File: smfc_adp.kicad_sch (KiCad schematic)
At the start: 22 parts, among them U1 ADP5091

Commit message: WIP
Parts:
- added J1, J2, J3: Conn_01x04_Socket, Connector_PinHeader_2.54mm:PinHeader_1x04_P2.54mm_Vertical, symbol Connector:Conn_01x04_Socket
- added JP1, JP2: SolderJumper_3_Bridged12, Jumper:SolderJumper-3_P1.3mm_Bridged12_Pad1.0x1.5mm, symbol Jumper:SolderJumper_3_Bridged12
- added R1: 55.6k, Resistor_SMD:R_0603_1608Metric_Pad0.98x0.95mm_HandSolder, symbol Device:R_US
- C1, C2, C3, C4, C5, C6, C?: footprint (none) -> Capacitor_SMD:C_0603_1608Metric_Pad1.08x0.95mm_HandSolder
- R10: renamed from R9; footprint (none) -> Resistor_SMD:R_0603_1608Metric_Pad0.98x0.95mm_HandSolder
- R11: renamed from R10; footprint (none) -> Resistor_SMD:R_0603_1608Metric_Pad0.98x0.95mm_HandSolder
- R12: renamed from R11; footprint (none) -> Resistor_SMD:R_0603_1608Metric_Pad0.98x0.95mm_HandSolder
- R13: renamed from R12; footprint (none) -> Resistor_SMD:R_0603_1608Metric_Pad0.98x0.95mm_HandSolder
- R14: renamed from R13; footprint (none) -> Resistor_SMD:R_0603_1608Metric_Pad0.98x0.95mm_HandSolder
- R2: renamed from R1; footprint (none) -> Resistor_SMD:R_0603_1608Metric_Pad0.98x0.95mm_HandSolder
- R3: renamed from R2; footprint (none) -> Resistor_SMD:R_0603_1608Metric_Pad0.98x0.95mm_HandSolder
- R4: renamed from R3; footprint (none) -> Resistor_SMD:R_0603_1608Metric_Pad0.98x0.95mm_HandSolder
- R5: renamed from R4; footprint (none) -> Resistor_SMD:R_0603_1608Metric_Pad0.98x0.95mm_HandSolder
- R6: renamed from R5; footprint (none) -> Resistor_SMD:R_0603_1608Metric_Pad0.98x0.95mm_HandSolder
- R7: renamed from R6; footprint (none) -> Resistor_SMD:R_0603_1608Metric_Pad0.98x0.95mm_HandSolder
- R8: renamed from R7; footprint (none) -> Resistor_SMD:R_0603_1608Metric_Pad0.98x0.95mm_HandSolder
- R9: renamed from R8; footprint (none) -> Resistor_SMD:R_0603_1608Metric_Pad0.98x0.95mm_HandSolder
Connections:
- net +BATT: now also J1.1 (Pin_1), J1.2 (Pin_2)
- net GND: now also J1.3 (Pin_3), J1.4 (Pin_4), J3.1 (Pin_1), J3.2 (Pin_2), J3.3 (Pin_3), J3.4 (Pin_4), JP1.3 (B), JP2.2 (C), R1.1; no longer U1.24 (REG_D0)
- net SYS: now also JP1.2 (C), JP2.3 (B); no longer U1.23 (REG_D1)
- net V_{ADP}: now also J2.1 (Pin_1), J2.2 (Pin_2), J2.3 (Pin_3), J2.4 (Pin_4)
- net at U1.20 (VID): now also R1.2
- new net: JP1.1 (A), U1.23 (REG_D1)
- new net: JP2.1 (A), U1.24 (REG_D0)
- no-connect marks 4 -> 3
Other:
- note added: "18/(18+4.7) = 0.793 MPPT set-point configured to around 80% of open circuit voltage"
- note added: "I need to confirm, but I think we can disable the regulated output by setting REG_D1 and D2 to GND"
- note added: "REG_FB is unused, effectively, as we're using VID to set the voltage for REG_OUT (that said, do we just want to disable REG_OUT?)."
- note added: "Settings for all of the control pins: SETSD - Sets shutdown discharge voltage on BAT pin - ~1.011 * (5.9 / 4.12 + 1) = between 2.32, 2.59 V due to V_{INT_REF} tolerance While BAT voltage < SETSD setpoint, converter is in async mode SETBK - Sets backup voltage enable threshold - ~ 1.011 * (6.04/4.02 + 1) = between 2.39 and 2.67 V due to V_{INT_REF} While BAT voltage < SETBK setpoint, backup batter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"
- note added: "Should we experiment and try powering our system from SYS instead of BAT? SYS is what charges up BAT."
- note added: "VID: floating, it sets reg output to 2.5V. Use a 55.6k resistor to set it to 3.3V."

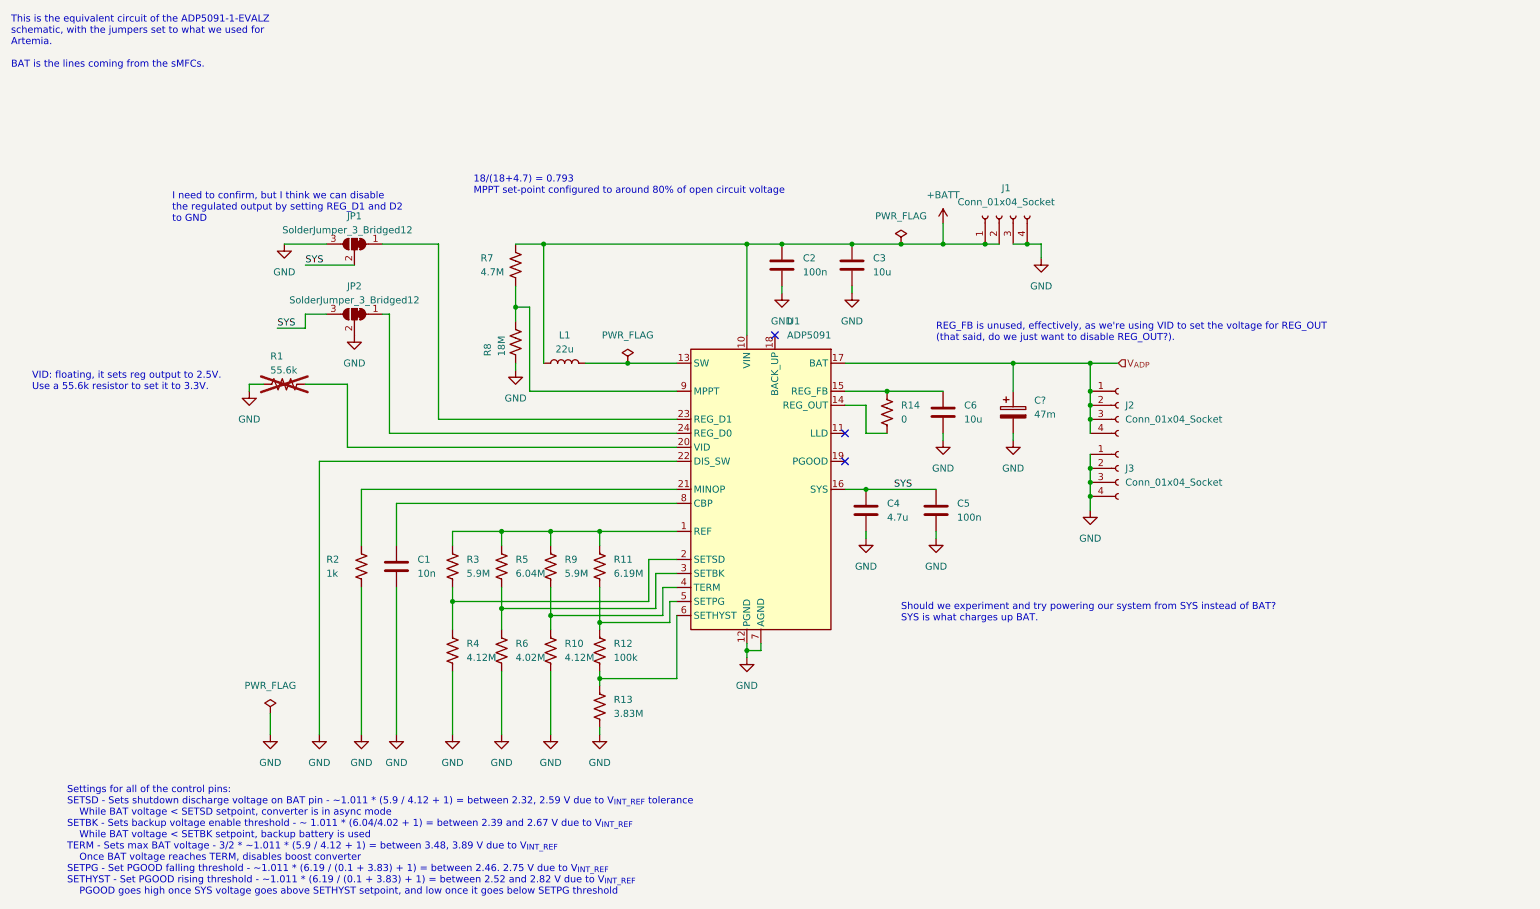
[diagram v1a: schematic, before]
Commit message: Layout cleanups, add more component data
 - Selected part for USB C socket
 - Tried to make more of the schematics compact and modular
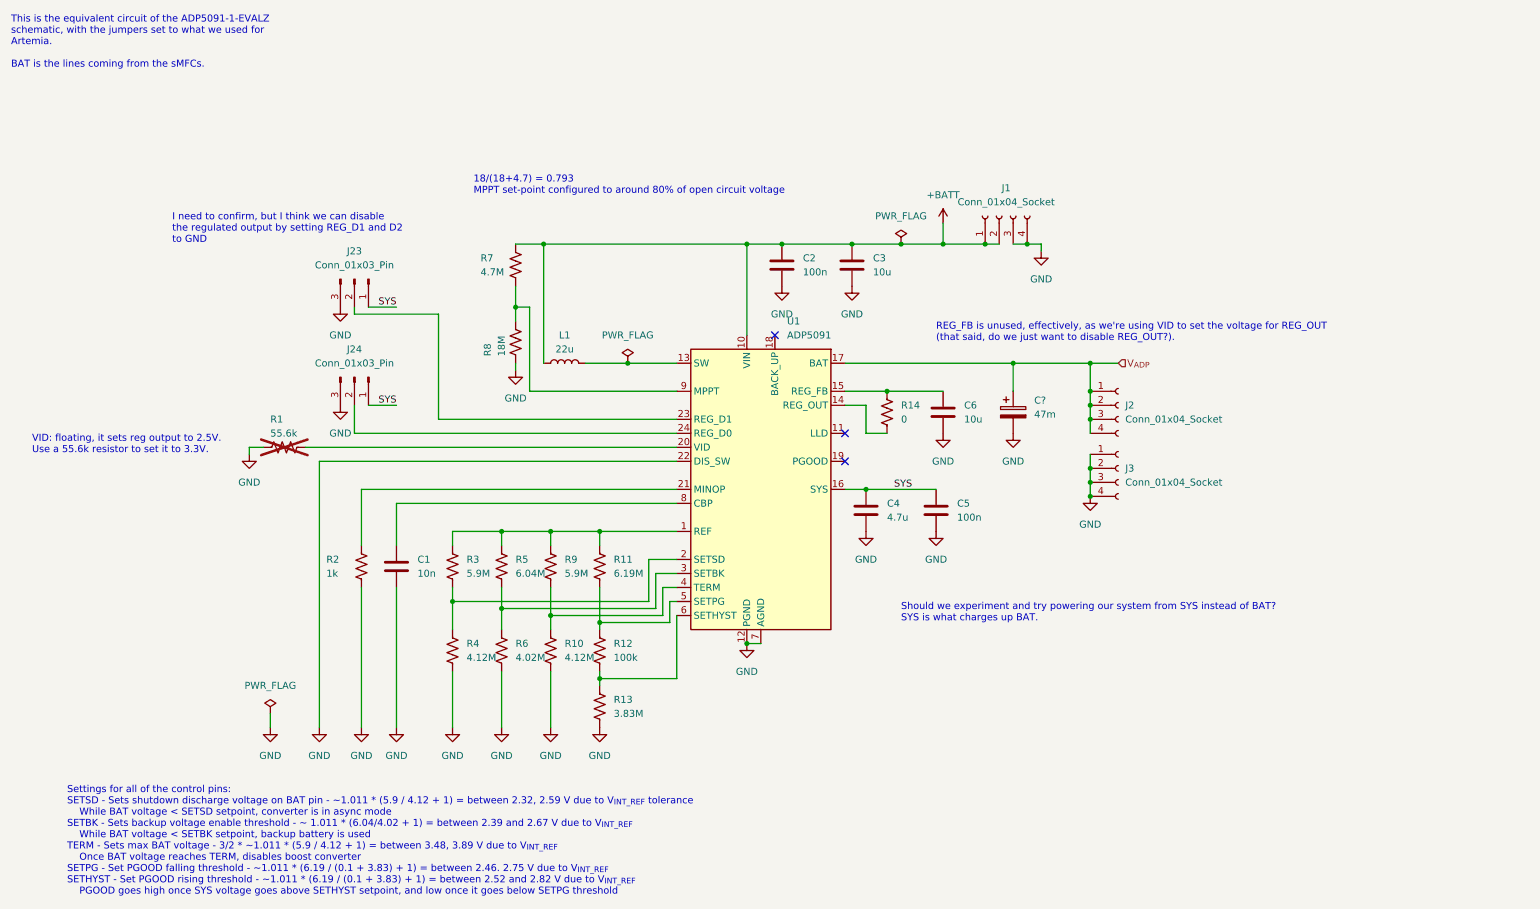
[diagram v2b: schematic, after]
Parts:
- removed JP1, JP2: SolderJumper_3_Bridged12, Jumper:SolderJumper-3_P1.3mm_Bridged12_Pad1.0x1.5mm, symbol Jumper:SolderJumper_3_Bridged12
- added J23, J24: Conn_01x03_Pin, Connector_PinHeader_2.54mm:PinHeader_1x03_P2.54mm_Vertical, symbol Connector:Conn_01x03_Pin
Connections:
- net GND: now also J23.3 (Pin_3), J24.3 (Pin_3)
- net SYS: now also J23.1 (Pin_1), J24.1 (Pin_1)
- net at U1.23 (REG_D1): now also J23.2 (Pin_2)
- net at U1.24 (REG_D0): now also J24.2 (Pin_2)
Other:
- moved on the sheet: R1

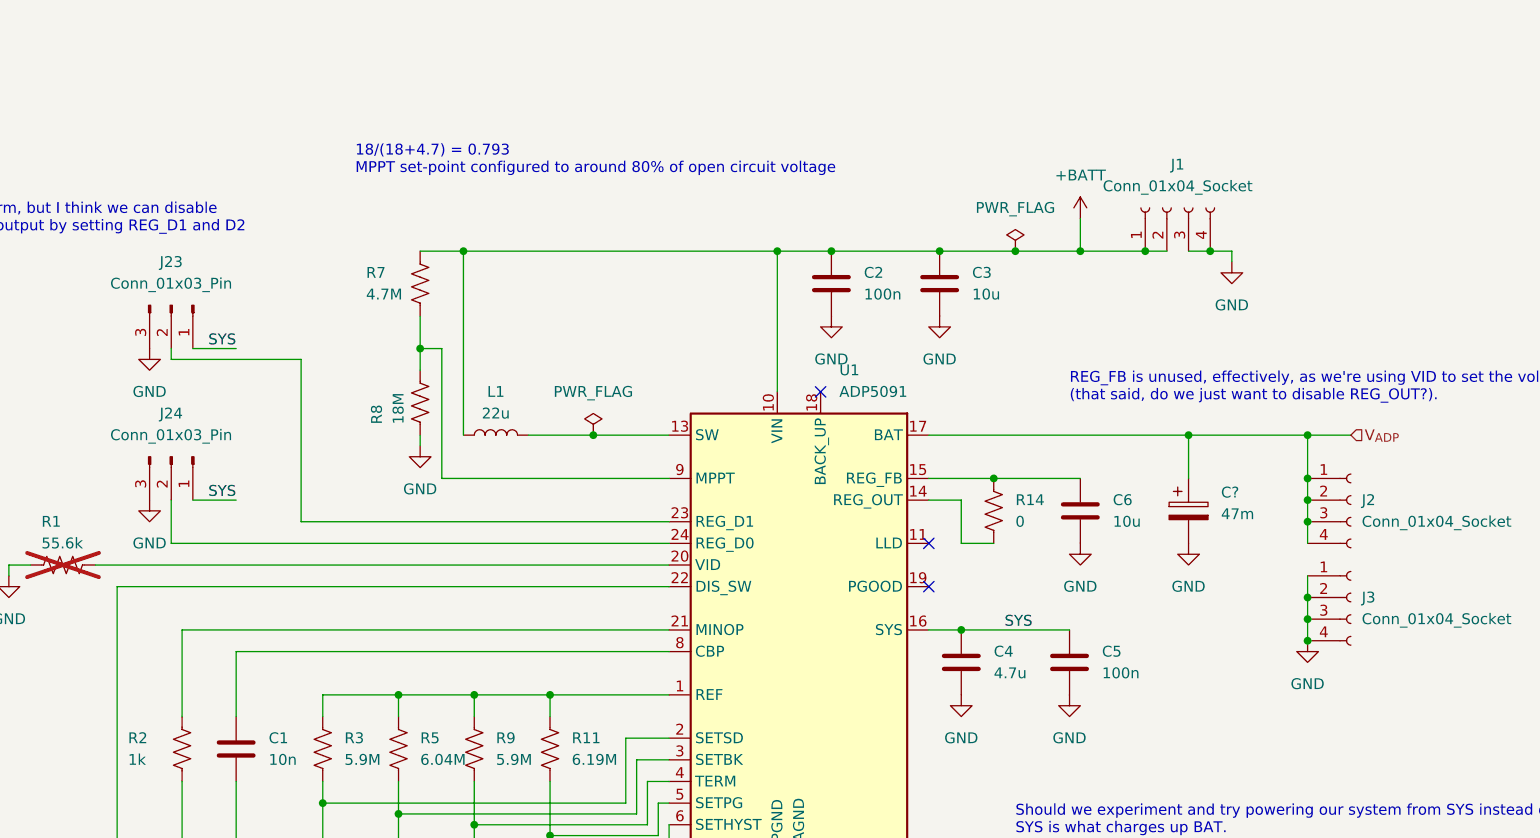
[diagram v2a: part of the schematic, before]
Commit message: First routing attempt
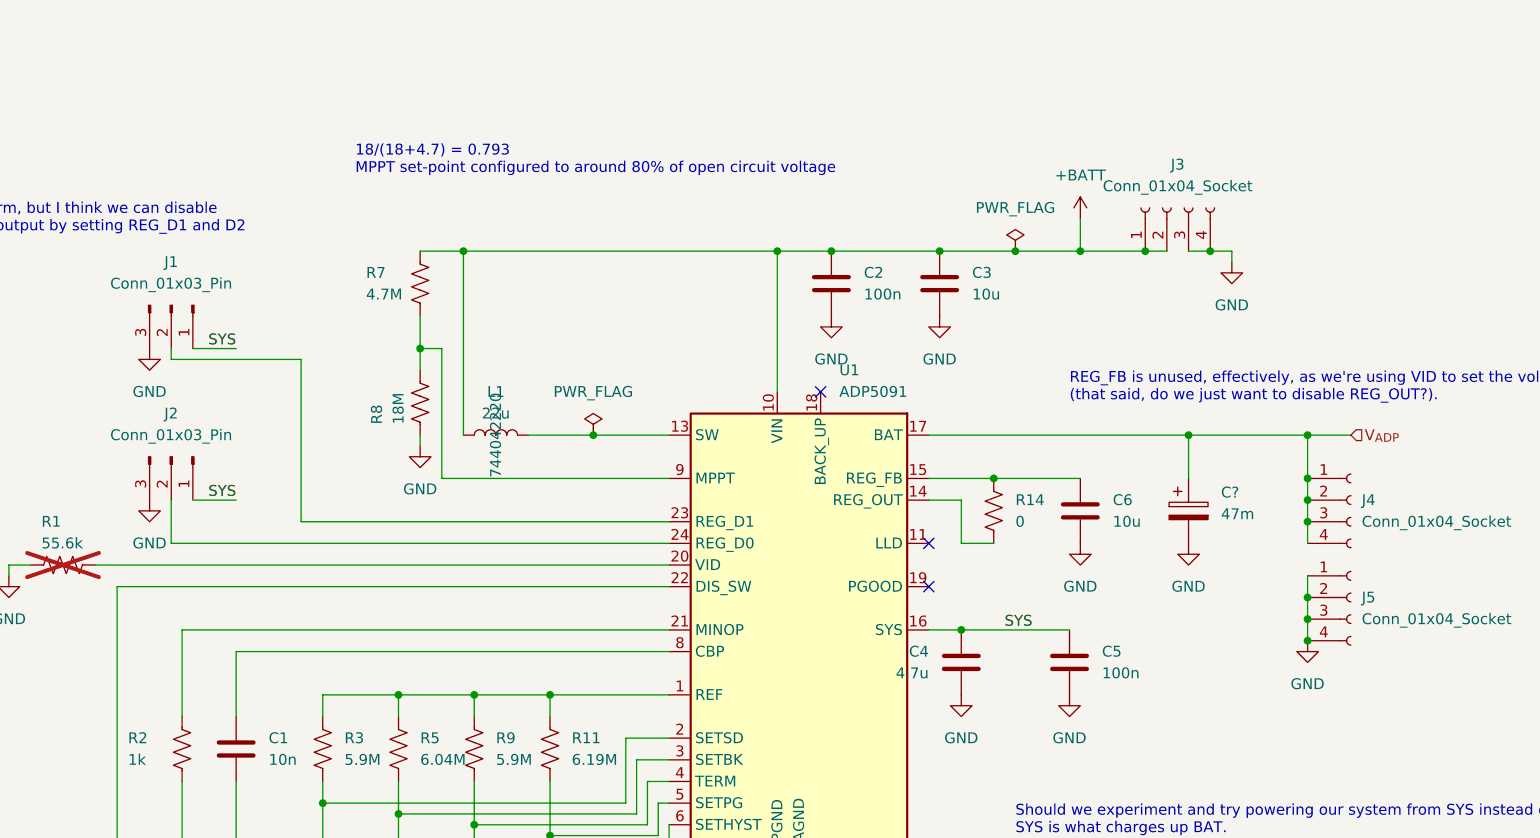
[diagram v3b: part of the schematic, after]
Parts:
- C?: footprint Capacitor_SMD:C_0603_1608Metric_Pad1.08x0.95mm_HandSolder -> Capacitor_THT:CP_Radial_D4.0mm_P1.50mm
- L1: footprint (none) -> Marcano:744042220; Digikey Product Number (none) -> 732-3657-1-ND; Manufacturer Product Number (none) -> 744042220
- renumbered J23 to J1, J24 to J2, J1 to J3, J2 to J4, J3 to J5
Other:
- moved on the sheet: C4
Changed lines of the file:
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@@
   (symbol (lib_id "power:GND") (at 73.66 67.31 0) (unit 1)
     (in_bom yes) (on_board yes) (dnp no) (fields_autoplaced)
-    (property "Reference" "#PWR03" (at 73.66 73.66 0)
+    (property "Reference" "#PWR04" (at 73.66 73.66 0)
       (effects (font (size 1.27 1.27)) hide)
     )
@@
       (project "artemia"
         (path "/3ef271cf-72c1-43e9-bc06-d7d78e288e38/251739c3-eec7-4a3d-b3c7-a06d817e60a9"
-          (reference "#PWR03") (unit 1)
+          (reference "#PWR04") (unit 1)
         )
       )
@@
   (symbol (lib_id "Connector:Conn_01x03_Pin") (at 76.2 80.01 270) (unit 1)
     (in_bom yes) (on_board yes) (dnp no) (fields_autoplaced)
-    (property "Reference" "J24" (at 76.2 74.93 90)
+    (property "Reference" "J2" (at 76.2 74.93 90)
       (effects (font (size 1.27 1.27)))
     )
@@
       (project "artemia"
         (path "/3ef271cf-72c1-43e9-bc06-d7d78e288e38/251739c3-eec7-4a3d-b3c7-a06d817e60a9"
-          (reference "J24") (unit 1)
+          (reference "J2") (unit 1)
         )
       )
@@
   (symbol (lib_id "Connector:Conn_01x03_Pin") (at 76.2 62.23 270) (unit 1)
     (in_bom yes) (on_board yes) (dnp no) (fields_autoplaced)
-    (property "Reference" "J23" (at 76.2 57.15 90)
+    (property "Reference" "J1" (at 76.2 57.15 90)
       (effects (font (size 1.27 1.27)))
     )
@@
       (project "artemia"
         (path "/3ef271cf-72c1-43e9-bc06-d7d78e288e38/251739c3-eec7-4a3d-b3c7-a06d817e60a9"
-          (reference "J23") (unit 1)
+          (reference "J1") (unit 1)
         )
       )
@@
       (effects (font (size 1.27 1.27)))
     )
-    (property "Footprint" "" (at 114.3 77.47 0)
-      (effects (font (size 1.27 1.27)) hide)
-    )
-    (property "Datasheet" "~" (at 114.3 77.47 0)
+    (property "Footprint" "Marcano:744042220" (at 114.3 77.47 0)
+      (effects (font (size 1.27 1.27)) hide)
+    )
+    (property "Datasheet" "https://www.we-online.com/components/products/datasheet/744042220.pdf" (at 114.3 77.47 0)
+      (effects (font (size 1.27 1.27)) hide)
+    )
+    (property "Manufacturer Product Number" "744042220" (at 114.3 77.47 0)
+      (effects (font (size 1.27 1.27)))
+    )
+    (property "Digikey Product Number" "732-3657-1-ND" (at 114.3 77.47 0)
+      (effects (font (size 1.27 1.27)) hide)
+    )
+    (property "Mouser Product Number" "" (at 114.3 77.47 0)
       (effects (font (size 1.27 1.27)) hide)
     )
@@
   (symbol (lib_id "power:GND") (at 69.85 143.51 0) (unit 1)
     (in_bom yes) (on_board yes) (dnp no) (fields_autoplaced)
-    (property "Reference" "#PWR04" (at 69.85 149.86 0)
+    (property "Reference" "#PWR03" (at 69.85 149.86 0)
       (effects (font (size 1.27 1.27)) hide)
     )
@@
       (project "artemia"
         (path "/3ef271cf-72c1-43e9-bc06-d7d78e288e38/251739c3-eec7-4a3d-b3c7-a06d817e60a9"
-          (reference "#PWR04") (unit 1)
+          (reference "#PWR03") (unit 1)
         )
       )
@@
     )
   )
-  (symbol (lib_id "Device:C") (at 168.91 104.14 180) (unit 1)
-    (in_bom yes) (on_board yes) (dnp no) (fields_autoplaced)
-    (property "Reference" "C4" (at 172.72 102.87 0)
-      (effects (font (size 1.27 1.27)) (justify right))
-    )
-    (property "Value" "4.7u" (at 172.72 105.41 0)
-      (effects (font (size 1.27 1.27)) (justify right))
-    )
-    (property "Footprint" "Capacitor_SMD:C_0603_1608Metric_Pad1.08x0.95mm_HandSolder" (at 167.9448 100.33 0)
+  (symbol (lib_id "Device:C") (at 168.91 104.14 0) (mirror x) (unit 1)
+    (in_bom yes) (on_board yes) (dnp no)
+    (property "Reference" "C4" (at 165.1 102.87 0)
+      (effects (font (size 1.27 1.27)) (justify right))
+    )
+    (property "Value" "4.7u" (at 165.1 105.41 0)
+      (effects (font (size 1.27 1.27)) (justify right))
+    )
+    (property "Footprint" "Capacitor_SMD:C_0603_1608Metric_Pad1.08x0.95mm_HandSolder" (at 169.8752 100.33 0)
       (effects (font (size 1.27 1.27)) hide)
     )
@@
   (symbol (lib_id "Connector:Conn_01x04_Socket") (at 214.63 85.09 0) (unit 1)
     (in_bom yes) (on_board yes) (dnp no) (fields_autoplaced)
-    (property "Reference" "J2" (at 215.9 85.09 0)
+    (property "Reference" "J4" (at 215.9 85.09 0)
       (effects (font (size 1.27 1.27)) (justify left))
     )
@@
       (project "artemia"
         (path "/3ef271cf-72c1-43e9-bc06-d7d78e288e38/251739c3-eec7-4a3d-b3c7-a06d817e60a9"
-          (reference "J2") (unit 1)
+          (reference "J4") (unit 1)
         )
       )
@@
   (symbol (lib_id "Connector:Conn_01x04_Socket") (at 193.04 50.8 90) (unit 1)
     (in_bom yes) (on_board yes) (dnp no) (fields_autoplaced)
-    (property "Reference" "J1" (at 194.31 45.72 90)
+    (property "Reference" "J3" (at 194.31 45.72 90)
       (effects (font (size 1.27 1.27)))
     )
@@
       (project "artemia"
         (path "/3ef271cf-72c1-43e9-bc06-d7d78e288e38/251739c3-eec7-4a3d-b3c7-a06d817e60a9"
-          (reference "J1") (unit 1)
+          (reference "J3") (unit 1)
         )
       )
@@
   (symbol (lib_id "Connector:Conn_01x04_Socket") (at 214.63 96.52 0) (unit 1)
     (in_bom yes) (on_board yes) (dnp no) (fields_autoplaced)
-    (property "Reference" "J3" (at 215.9 96.52 0)
+    (property "Reference" "J5" (at 215.9 96.52 0)
       (effects (font (size 1.27 1.27)) (justify left))
     )
@@
       (project "artemia"
         (path "/3ef271cf-72c1-43e9-bc06-d7d78e288e38/251739c3-eec7-4a3d-b3c7-a06d817e60a9"
-          (reference "J3") (unit 1)
+          (reference "J5") (unit 1)
         )
       )
@@
       (effects (font (size 1.27 1.27)) (justify left))
     )
-    (property "Footprint" "Capacitor_SMD:C_0603_1608Metric_Pad1.08x0.95mm_HandSolder" (at 196.5452 90.17 0)
+    (property "Footprint" "Capacitor_THT:CP_Radial_D4.0mm_P1.50mm" (at 196.5452 90.17 0)
       (effects (font (size 1.27 1.27)) hide)
     )
@@
       (effects (font (size 1.27 1.27)) hide)
     )
+    (property "Manufacturer Product Number" "" (at 195.58 86.36 0)
+      (effects (font (size 1.27 1.27)))
+    )
+    (property "Digikey Product Number" "" (at 195.58 86.36 0)
+      (effects (font (size 1.27 1.27)) hide)
+    )
+    (property "Mouser Product Number" "" (at 195.58 86.36 0)
+      (effects (font (size 1.27 1.27)) hide)
+    )
